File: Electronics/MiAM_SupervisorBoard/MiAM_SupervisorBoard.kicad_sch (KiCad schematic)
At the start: 3 parts, among them J1 ST7789_TFT_Screen, U1 WT32-ETH01, U2 ESP32-CAM

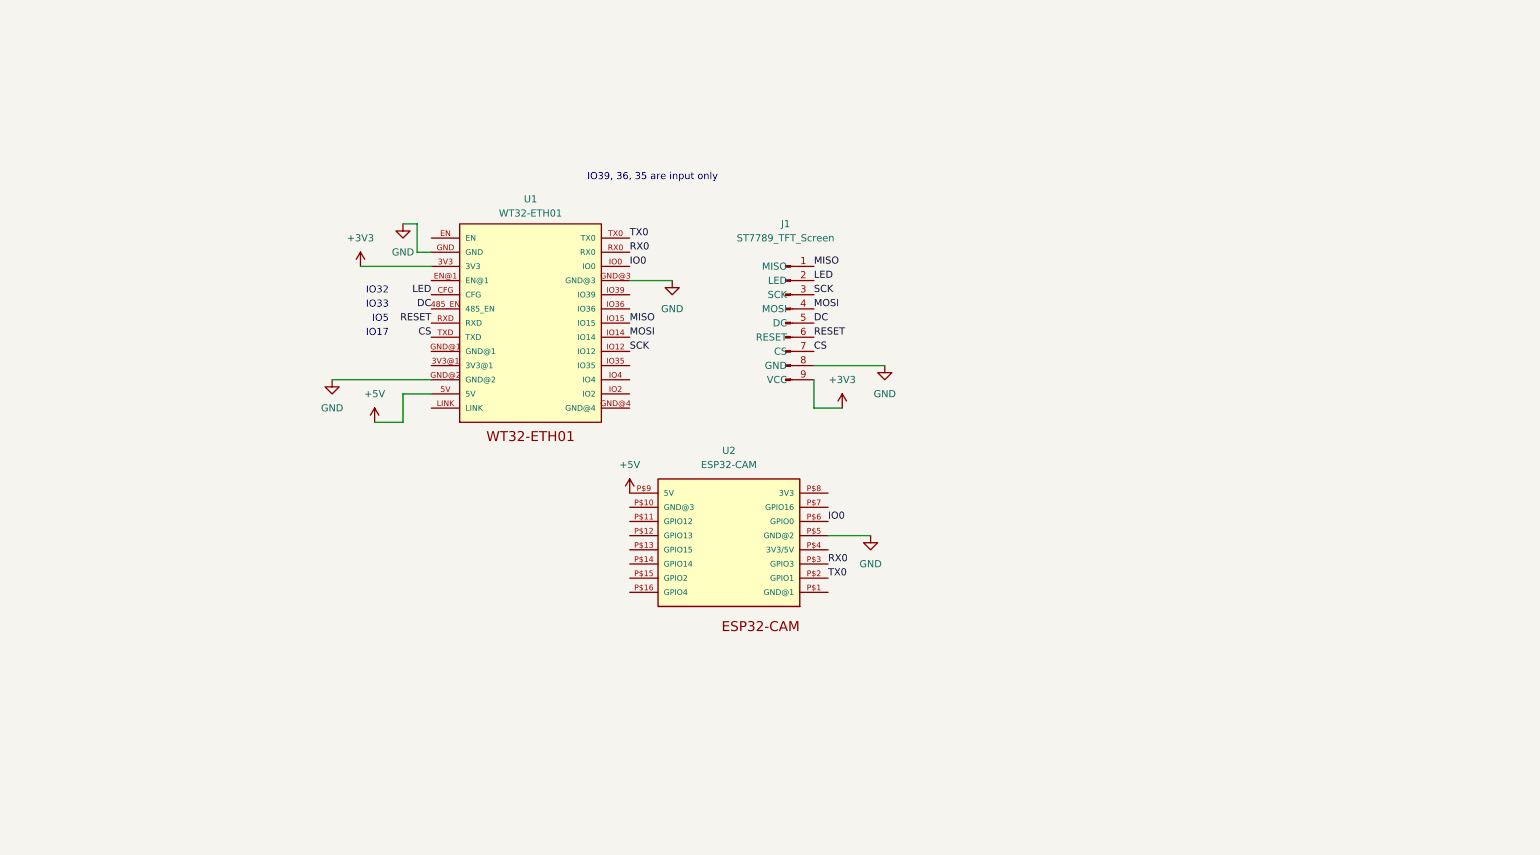
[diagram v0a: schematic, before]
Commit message: Complete supervisor PCB
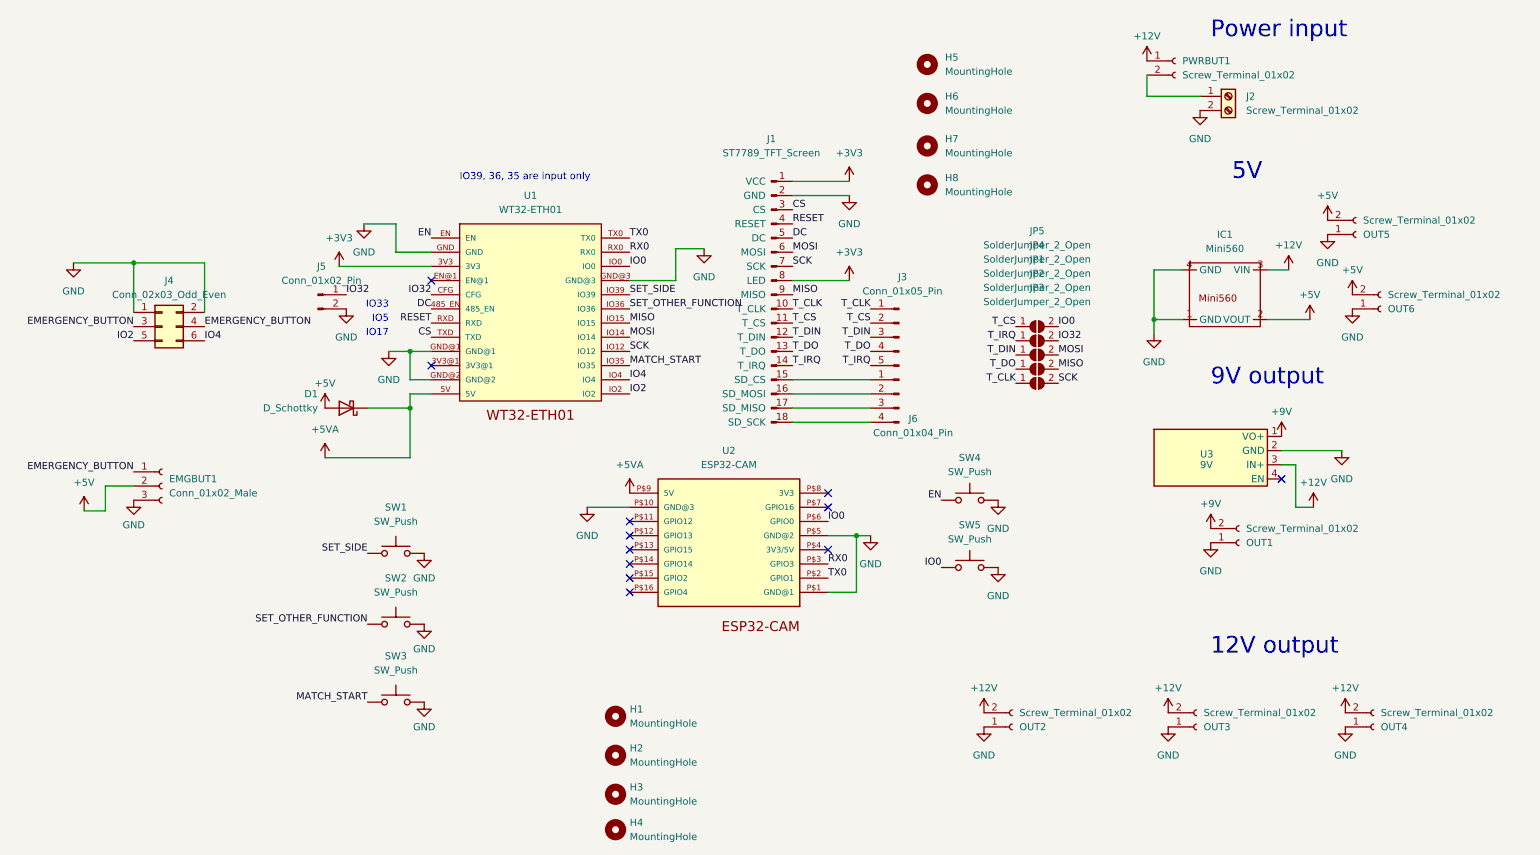
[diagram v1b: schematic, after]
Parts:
- added D1: D_Schottky, Diode_SMD:D_SOD-323_HandSoldering, symbol Device:D_Schottky
- added EMGBUT1: Conn_01x02_Male, Connector_JST:JST_PH_B3B-PH-K_1x03_P2.00mm_Vertical, symbol Connector:Conn_01x03_Female
- added H1, H2, H3, H4: MountingHole, MountingHole:MountingHole_3.2mm_M3, symbol Mechanical:MountingHole
- added H5, H6, H7, H8: MountingHole, MountingHole:MountingHole_2.7mm_M2.5, symbol Mechanical:MountingHole
- added IC1: Mini560, MiAM_ESP32_Footprints:Mini560, symbol Mini560:Mini560
- added J2: Screw_Terminal_01x02, MiAM_ESP32_Footprints:USBC-Dummy-Card, symbol Connector:Screw_Terminal_01x02
- added J3: Conn_01x05_Pin, Connector_PinHeader_2.54mm:PinHeader_1x05_P2.54mm_Vertical, symbol Connector:Conn_01x05_Pin
- added J4: Conn_02x03_Odd_Even, Connector_PinHeader_2.54mm:PinHeader_2x03_P2.54mm_Vertical, symbol Connector_Generic:Conn_02x03_Odd_Even
- added J5: Conn_01x02_Pin, Connector_PinHeader_2.54mm:PinHeader_1x02_P2.54mm_Vertical, symbol Connector:Conn_01x02_Pin
- added J6: Conn_01x04_Pin, Connector_PinHeader_2.54mm:PinHeader_1x04_P2.54mm_Vertical, symbol Connector:Conn_01x04_Pin
- added JP1, JP2, JP3, JP4, JP5: SolderJumper_2_Open, Jumper:SolderJumper-2_P1.3mm_Open_RoundedPad1.0x1.5mm, symbol Jumper:SolderJumper_2_Open
- added OUT1, OUT2, OUT3, OUT4, OUT5, OUT6, PWRBUT1: Screw_Terminal_01x02, Connector_JST:JST_PH_B2B-PH-K_1x02_P2.00mm_Vertical, symbol Connector:Conn_01x02_Female
- added SW1, SW2, SW3: SW_Push, Connector_JST:JST_PH_B2B-PH-K_1x02_P2.00mm_Vertical, symbol Switch:SW_Push
- added SW4, SW5: SW_Push, Button_Switch_SMD:SW_Push_1P1T_NO_Vertical_Wuerth_434133025816, symbol Switch:SW_Push
- added U3: 9V, MiAM_ESP32_Footprints:VoltageRegulator, symbol MiAM_ESP32:VoltageRegulator
- J1: footprint (none) -> MiAM_ESP32_Footprints:2.8_tft_240x320_touch_sd_spi
- U1: footprint WT32-ETH01:WT32-ETH01 -> MiAM_ESP32_Footprints:WT32-ETH01-MB; symbol WT32-ETH01:WT32-ETH01 -> WT32-ETH01:WT32-ETH01_MB
- U2: footprint ESP32-CAM:ESP32-CAM -> MiAM_ESP32_Footprints:ESP32-CAM_MB
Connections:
- net +3V3: now also J1.1 (VCC), J1.8 (LED); no longer J1.9 (VCC)
- net +5V: now also D1.2 (A), EMGBUT1.2 (Pin_2), IC1.2 (VOUT), OUT5.2 (Pin_2), OUT6.2 (Pin_2); no longer U1.5V, U2.P$9 (5V)
- net CS: now also J1.3 (CS); no longer J1.7 (CS)
- net GND: now also J1.2 (GND), U1.GND@1, U2.P$1 (GND@1), U2.P$10 (GND@3), EMGBUT1.3 (Pin_3), IC1.1 (GND), IC1.4 (GND), J2.2 (Pin_2), J4.1 (Pin_1), J4.2 (Pin_2), J5.2 (Pin_2), OUT1.1 (Pin_1), OUT2.1 (Pin_1), OUT3.1 (Pin_1), OUT4.1 (Pin_1), OUT5.1 (Pin_1), OUT6.1 (Pin_1), SW1.2, SW2.2, SW3.2, SW4.2, SW5.2, U3.2 (GND); no longer J1.8 (GND)
- net IO0: now also JP5.2 (B), SW5.1
- net MISO: now also J1.9 (MISO), JP2.2 (B); no longer J1.1 (MISO)
- net MOSI: now also J1.6 (MOSI), JP1.2 (B); no longer J1.4 (MOSI)
- net RESET: now also J1.4 (RESET); no longer J1.6 (RESET)
- net SCK: now also J1.7 (SCK), JP3.2 (B); no longer J1.3 (SCK)
- net EN: now reaches U1.EN
- net EN: now also SW4.1
- net IO2: now reaches U1.IO2
- net IO2: now also J4.5 (Pin_5)
- net MATCH_START: now reaches U1.IO35
- net MATCH_START: now also SW3.1
- net SET_OTHER_FUNCTION: now reaches U1.IO36
- net SET_OTHER_FUNCTION: now also SW2.1
- net SET_SIDE: now reaches U1.IO39
- net SET_SIDE: now also SW1.1
- net IO4: now reaches U1.IO4
- net IO4: now also J4.6 (Pin_6)
- net LED renamed IO32
- net IO32: now also J5.1 (Pin_1), JP4.2 (B); no longer J1.2 (LED)
- new net: J1.15 (SD_CS), J6.1 (Pin_1)
- new net: J1.16 (SD_MOSI), J6.2 (Pin_2)
- new net: J1.17 (SD_MISO), J6.3 (Pin_3)
- new net: J1.18 (SD_SCK), J6.4 (Pin_4)
- new net: J2.1 (Pin_1), PWRBUT1.2 (Pin_2)
- new net +12V: IC1.3 (VIN), OUT2.2 (Pin_2), OUT3.2 (Pin_2), OUT4.2 (Pin_2), PWRBUT1.1 (Pin_1), U3.3 (IN+)
- new net +5VA: D1.1 (K), U1.5V, U2.P$9 (5V)
- new net +9V: OUT1.2 (Pin_2), U3.1 (VO+)
- new net EMERGENCY_BUTTON: EMGBUT1.1 (Pin_1), J4.3 (Pin_3), J4.4 (Pin_4)
- new net T_CLK: J1.10 (T_CLK), J3.1 (Pin_1), JP3.1 (A)
- new net T_CS: J1.11 (T_CS), J3.2 (Pin_2), JP5.1 (A)
- new net T_DIN: J1.12 (T_DIN), J3.3 (Pin_3), JP1.1 (A)
- new net T_DO: J1.13 (T_DO), J3.4 (Pin_4), JP2.1 (A)
- new net T_IRQ: J1.14 (T_IRQ), J3.5 (Pin_5), JP4.1 (A)
- no-connect marks 0 -> 12
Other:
- note added: "12V output"
- note added: "5V"
- note added: "9V output"
- note added: "Power input"
- note removed: "IO32"
